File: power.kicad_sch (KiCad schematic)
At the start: 55 parts, among them Q1 AO3401A, Q2 AO3401A, Q21 FS8205A, Q6 2N7002, U10 BQ27546, U27 TPS63001, U29 BQ24081, U30 DW01+G, U6 TPS61040DBV

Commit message: Finish ESP32 fanout
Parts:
- added C41: 10uF, Capacitor_SMD:C_0402_1005Metric, symbol Device:C_Small
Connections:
- net GND: now also C41.1
- net at C41.2, D3.1 (K), Q1.2 (S)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: now also C41.2
- net VUSB renamed VBUS
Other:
- moved on the sheet: C41, C42, C43, L1, R9, U27

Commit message: Finish first layout revision
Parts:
- added R22: 100R, Resistor_SMD:R_0402_1005Metric, symbol Device:R_Small
- R22: footprint Resistor_SMD:R_0603_1608Metric -> Resistor_SMD:R_0402_1005Metric; LCSC C23179 -> C25117
- U10: footprint Package_DSBGA:DSBGA-15_1.95x2.6mm_P0.5mm -> Package_DSBGA:DSBGA-15_BQ27546_1.95x2.6mm_P0.5mm
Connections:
- net GND: now also U29.8 (~{TE})
- net VBUS: no longer U29.8 (~{TE})
- net at Q21.4, U30.1 (DO): now also R22.1
- net at C48.1, R22.2, U10.E1 (REGIN): no longer U10.D2 (CE)
- net at C48.1, C48.2, R22.2: now also U10.B1 (SRN); no longer U10.A2 (SRN)
- new net DSG: R22.2, U10.D2 (CE)
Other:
- moved on the sheet: C38, C47, R20

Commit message: Make EDRC happy (mostly)
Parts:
- C38: symbol Device:CP -> Device:C_Polarized
- FB1: symbol Device:Ferrite_Bead_Small -> Device:FerriteBead_Small
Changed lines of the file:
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@@
 (kicad_sch (version 20230121) (generator eeschema)
   (paper "A4")
+  (junction (at 148.59 143.51) (diameter 0) (color 0 0 0 0)
+  )
   (junction (at 101.6 163.83) (diameter 0) (color 0 0 0 0)
   )
@@
   (junction (at 172.72 163.83) (diameter 0) (color 0 0 0 0)
   )
-  (junction (at 115.57 46.99) (diameter 0) (color 0 0 0 0)
-  )
   (junction (at 38.1 46.99) (diameter 0) (color 0 0 0 0)
   )
@@
     (stroke (width 0) (type default))
   )
+  (wire (pts (xy 247.65 92.71) (xy 247.65 93.98))
+    (stroke (width 0) (type default))
+  )
   (wire (pts (xy 167.64 46.99) (xy 195.58 46.99))
     (stroke (width 0) (type default))
@@
     (stroke (width 0) (type default))
   )
-  (wire (pts (xy 137.16 143.51) (xy 151.13 143.51))
+  (wire (pts (xy 137.16 143.51) (xy 148.59 143.51))
+    (stroke (width 0) (type default))
+  )
+  (wire (pts (xy 148.59 142.24) (xy 148.59 143.51))
     (stroke (width 0) (type default))
   )
@@
     (stroke (width 0) (type default))
   )
-  (wire (pts (xy 151.13 154.94) (xy 151.13 163.83))
+  (wire (pts (xy 148.59 143.51) (xy 151.13 143.51))
     (stroke (width 0) (type default))
   )
-  (wire (pts (xy 115.57 38.1) (xy 115.57 46.99))
+  (wire (pts (xy 151.13 154.94) (xy 151.13 163.83))
     (stroke (width 0) (type default))
   )
@@
     (stroke (width 0) (type default))
   )
-  (wire (pts (xy 115.57 46.99) (xy 127 46.99))
+  (wire (pts (xy 142.24 86.36) (xy 142.24 87.63))
     (stroke (width 0) (type default))
   )
@@
     (stroke (width 0) (type default))
   )
+  (wire (pts (xy 207.01 81.28) (xy 207.01 82.55))
+    (stroke (width 0) (type default))
+  )
   (wire (pts (xy 240.03 46.99) (xy 250.19 46.99))
     (stroke (width 0) (type default))
@@
     (stroke (width 0) (type default))
   )
-  (wire (pts (xy 250.19 45.72) (xy 250.19 46.99))
-    (stroke (width 0) (type default))
-  )
   (wire (pts (xy 88.9 172.72) (xy 88.9 171.45))
     (stroke (width 0) (type default))
@@
     (stroke (width 0) (type default))
   )
-  (wire (pts (xy 106.68 46.99) (xy 115.57 46.99))
+  (wire (pts (xy 142.24 87.63) (xy 137.16 87.63))
+    (stroke (width 0) (type default))
+  )
+  (wire (pts (xy 106.68 46.99) (xy 127 46.99))
     (stroke (width 0) (type default))
   )
@@
     )
   )
-  (symbol (lib_id "Device:CP") (at 27.94 52.07 0) (unit 1)
+  (symbol (lib_id "Device:C_Polarized") (at 27.94 52.07 0) (unit 1)
     (in_bom yes) (on_board yes) (dnp no)
     (property "Reference" "C38" (at 30.9372 50.9016 0)
@@
     )
   )
-  (symbol (lib_name "+BATT_1") (lib_id "power:+BATT") (at 106.68 38.1 0) (unit 1)
+  (symbol (lib_id "power:+BATT") (at 106.68 38.1 0) (unit 1)
     (in_bom yes) (on_board yes) (dnp no) (fields_autoplaced)
     (property "Reference" "#PWR051" (at 106.68 41.91 0)
@@
     )
   )
+  (symbol (lib_id "power:PWR_FLAG") (at 207.01 81.28 0) (unit 1)
+    (in_bom yes) (on_board yes) (dnp no) (fields_autoplaced)
+    (property "Reference" "#FLG04" (at 207.01 79.375 0)
+      (effects (font (size 1.27 1.27)) hide)
+    )
+    (property "Value" "PWR_FLAG" (at 207.01 77.7781 0)
+      (effects (font (size 1.27 1.27)))
+    )
+    (property "Footprint" "" (at 207.01 81.28 0)
+      (effects (font (size 1.27 1.27)) hide)
+    )
+    (property "Datasheet" "~" (at 207.01 81.28 0)
+      (effects (font (size 1.27 1.27)) hide)
+    )
+    (pin "1")
+    (instances
+      (project "oled-nametag"
+        (path "/c0b8a503-1da4-4e1a-941c-dddf39a5c519/b1f1b085-615b-4d75-b80e-4b089a5e74f7"
+          (reference "#FLG04") (unit 1)
+        )
+      )
+    )
+  )
   (symbol (lib_id "Device:C_Small") (at 118.11 109.22 0) (mirror y) (unit 1)
     (in_bom yes) (on_board yes) (dnp no)
@@
     )
   )
+  (symbol (lib_id "power:PWR_FLAG") (at 148.59 142.24 0) (unit 1)
+    (in_bom yes) (on_board yes) (dnp no) (fields_autoplaced)
+    (property "Reference" "#FLG08" (at 148.59 140.335 0)
+      (effects (font (size 1.27 1.27)) hide)
+    )
+    (property "Value" "PWR_FLAG" (at 148.59 138.7381 0)
+      (effects (font (size 1.27 1.27)))
+    )
+    (property "Footprint" "" (at 148.59 142.24 0)
+      (effects (font (size 1.27 1.27)) hide)
+    )
+    (property "Datasheet" "~" (at 148.59 142.24 0)
+      (effects (font (size 1.27 1.27)) hide)
+    )
+    (pin "1")
+    (instances
+      (project "oled-nametag"
+        (path "/c0b8a503-1da4-4e1a-941c-dddf39a5c519/b1f1b085-615b-4d75-b80e-4b089a5e74f7"
+          (reference "#FLG08") (unit 1)
+        )
+      )
+    )
+  )
   (symbol (lib_id "Device:C_Small") (at 207.01 86.36 0) (mirror x) (unit 1)
     (in_bom yes) (on_board yes) (dnp no) (fields_autoplaced)
@@
     )
   )
+  (symbol (lib_id "power:PWR_FLAG") (at 142.24 86.36 0) (unit 1)
+    (in_bom yes) (on_board yes) (dnp no) (fields_autoplaced)
+    (property "Reference" "#FLG03" (at 142.24 84.455 0)
+      (effects (font (size 1.27 1.27)) hide)
+    )
+    (property "Value" "PWR_FLAG" (at 142.24 82.8581 0)
+      (effects (font (size 1.27 1.27)))
+    )
+    (property "Footprint" "" (at 142.24 86.36 0)
+      (effects (font (size 1.27 1.27)) hide)
+    )
+    (property "Datasheet" "~" (at 142.24 86.36 0)
+      (effects (font (size 1.27 1.27)) hide)
+    )
+    (pin "1")
+    (instances
+      (project "oled-nametag"
+        (path "/c0b8a503-1da4-4e1a-941c-dddf39a5c519/b1f1b085-615b-4d75-b80e-4b089a5e74f7"
+          (reference "#FLG03") (unit 1)
+        )
+      )
+    )
+  )
   (symbol (lib_id "power:GND") (at 213.36 68.58 0) (unit 1)
     (in_bom yes) (on_board yes) (dnp no)
@@
     )
   )
-  (symbol (lib_id "power:PWR_FLAG") (at 250.19 45.72 0) (unit 1)
-    (in_bom yes) (on_board yes) (dnp no) (fields_autoplaced)
-    (property "Reference" "#FLG04" (at 250.19 43.815 0)
+  (symbol (lib_id "power:GND") (at 38.1 64.77 0) (unit 1)
+    (in_bom yes) (on_board yes) (dnp no)
+    (property "Reference" "#PWR0209" (at 38.1 71.12 0)
       (effects (font (size 1.27 1.27)) hide)
     )
-    (property "Value" "PWR_FLAG" (at 250.19 42.2181 0)
+    (property "Value" "GND" (at 38.227 69.1642 0)
       (effects (font (size 1.27 1.27)))
     )
-    (property "Footprint" "" (at 250.19 45.72 0)
+    (property "Footprint" "" (at 38.1 64.77 0)
       (effects (font (size 1.27 1.27)) hide)
     )
-    (property "Datasheet" "~" (at 250.19 45.72 0)
+    (property "Datasheet" "" (at 38.1 64.77 0)
       (effects (font (size 1.27 1.27)) hide)
     )
     (pin "1")
     (instances
+      (project "rgb-led-nametag-48x16"
+        (path "/751d823e-1d7b-4501-9658-d06d459b0e16"
+          (reference "#PWR0209") (unit 1)
+        )
+      )
       (project "oled-nametag"
         (path "/c0b8a503-1da4-4e1a-941c-dddf39a5c519/b1f1b085-615b-4d75-b80e-4b089a5e74f7"
-          (reference "#FLG04") (unit 1)
+          (reference "#PWR046") (unit 1)
         )
       )
     )
   )
-  (symbol (lib_id "power:GND") (at 38.1 64.77 0) (unit 1)
-    (in_bom yes) (on_board yes) (dnp no)
-    (property "Reference" "#PWR0209" (at 38.1 71.12 0)
+  (symbol (lib_id "power:PWR_FLAG") (at 247.65 92.71 0) (unit 1)
+    (in_bom yes) (on_board yes) (dnp no) (fields_autoplaced)
+    (property "Reference" "#FLG09" (at 247.65 90.805 0)
       (effects (font (size 1.27 1.27)) hide)
     )
-    (property "Value" "GND" (at 38.227 69.1642 0)
+    (property "Value" "PWR_FLAG" (at 247.65 89.2081 0)
       (effects (font (size 1.27 1.27)))
     )
-    (property "Footprint" "" (at 38.1 64.77 0)
+    (property "Footprint" "" (at 247.65 92.71 0)
       (effects (font (size 1.27 1.27)) hide)
     )
-    (property "Datasheet" "" (at 38.1 64.77 0)
+    (property "Datasheet" "~" (at 247.65 92.71 0)
       (effects (font (size 1.27 1.27)) hide)
     )
     (pin "1")
     (instances
-      (project "rgb-led-nametag-48x16"
-        (path "/751d823e-1d7b-4501-9658-d06d459b0e16"
-          (reference "#PWR0209") (unit 1)
-        )
-      )
       (project "oled-nametag"
         (path "/c0b8a503-1da4-4e1a-941c-dddf39a5c519/b1f1b085-615b-4d75-b80e-4b089a5e74f7"
-          (reference "#PWR046") (unit 1)
+          (reference "#FLG09") (unit 1)
         )
       )
@@
     )
   )
-  (symbol (lib_id "power:PWR_FLAG") (at 115.57 38.1 0) (unit 1)
-    (in_bom yes) (on_board yes) (dnp no) (fields_autoplaced)
-    (property "Reference" "#FLG03" (at 115.57 36.195 0)
-      (effects (font (size 1.27 1.27)) hide)
-    )
-    (property "Value" "PWR_FLAG" (at 115.57 34.5981 0)
-      (effects (font (size 1.27 1.27)))
-    )
-    (property "Footprint" "" (at 115.57 38.1 0)
-      (effects (font (size 1.27 1.27)) hide)
-    )
-    (property "Datasheet" "~" (at 115.57 38.1 0)
-      (effects (font (size 1.27 1.27)) hide)
-    )
-    (pin "1")
-    (instances
-      (project "oled-nametag"
-        (path "/c0b8a503-1da4-4e1a-941c-dddf39a5c519/b1f1b085-615b-4d75-b80e-4b089a5e74f7"
-          (reference "#FLG03") (unit 1)
-        )
-      )
-    )
-  )
   (symbol (lib_id "power:GND") (at 222.25 105.41 0) (unit 1)
     (in_bom yes) (on_board yes) (dnp no) (fields_autoplaced)
@@
     )
   )
-  (symbol (lib_id "Device:Ferrite_Bead_Small") (at 36.83 30.48 90) (unit 1)
+  (symbol (lib_id "Device:FerriteBead_Small") (at 36.83 30.48 90) (unit 1)
     (in_bom yes) (on_board yes) (dnp no)
     (property "Reference" "FB1" (at 35.6616 27.94 0)

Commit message: Add fuel gauge thermistor
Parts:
- added R21: 10k, Resistor_SMD:R_0402_1005Metric, symbol Device:R_Small
- U10: footprint Package_DSBGA:DSBGA-15_BQ27546_1.95x2.6mm_P0.5mm -> Package_DSBGA:DSBGA-15_BQ27546_I2C_1.95x2.6mm_P0.5mm
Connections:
- net GND: now also R21.2
- net at U10.B2 (TS): now also R21.1
- no-connect marks 4 -> 3
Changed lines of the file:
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@@
   )
   (no_connect (at 146.05 100.33))
-  (no_connect (at 128.27 115.57))
   (no_connect (at 146.05 95.25))
   (no_connect (at 161.29 168.91))
@@
   )
   (wire (pts (xy 237.49 33.02) (xy 237.49 41.91))
+    (stroke (width 0) (type default))
+  )
+  (wire (pts (xy 128.27 115.57) (xy 128.27 118.11))
     (stroke (width 0) (type default))
   )
@@
     )
   )
+  (symbol (lib_id "power:GND") (at 128.27 123.19 0) (mirror y) (unit 1)
+    (in_bom yes) (on_board yes) (dnp no)
+    (property "Reference" "#PWR0210" (at 128.27 129.54 0)
+      (effects (font (size 1.27 1.27)) hide)
+    )
+    (property "Value" "GND" (at 128.143 127.5842 0)
+      (effects (font (size 1.27 1.27)))
+    )
+    (property "Footprint" "" (at 128.27 123.19 0)
+      (effects (font (size 1.27 1.27)) hide)
+    )
+    (property "Datasheet" "" (at 128.27 123.19 0)
+      (effects (font (size 1.27 1.27)) hide)
+    )
+    (pin "1")
+    (instances
+      (project "rgb-led-nametag-48x16"
+        (path "/751d823e-1d7b-4501-9658-d06d459b0e16"
+          (reference "#PWR0210") (unit 1)
+        )
+      )
+      (project "oled-nametag"
+        (path "/c0b8a503-1da4-4e1a-941c-dddf39a5c519/b1f1b085-615b-4d75-b80e-4b089a5e74f7"
+          (reference "#PWR035") (unit 1)
+        )
+      )
+    )
+  )
   (symbol (lib_id "power:+BATT") (at 106.68 38.1 0) (unit 1)
     (in_bom yes) (on_board yes) (dnp no) (fields_autoplaced)
@@
       (effects (font (size 1.27 1.27)) (justify left))
     )
-    (property "Footprint" "Package_DSBGA:DSBGA-15_BQ27546_1.95x2.6mm_P0.5mm" (at 137.16 104.14 0)
+    (property "Footprint" "Package_DSBGA:DSBGA-15_BQ27546_I2C_1.95x2.6mm_P0.5mm" (at 137.16 104.14 0)
       (effects (font (size 1.27 1.27)) hide)
     )
@@
         )
       )
+    )
+  )
+  (symbol (lib_id "Device:R_Small") (at 128.27 120.65 0) (unit 1)
+    (in_bom yes) (on_board yes) (dnp no)
+    (property "Reference" "R21" (at 126.7714 119.4816 0)
+      (effects (font (size 1.27 1.27)) (justify right))
+    )
+    (property "Value" "10k" (at 126.7714 121.793 0)
+      (effects (font (size 1.27 1.27)) (justify right))
+    )
+    (property "Footprint" "Resistor_SMD:R_0402_1005Metric" (at 128.27 120.65 0)
+      (effects (font (size 1.27 1.27)) hide)
+    )
+    (property "Datasheet" "~" (at 128.27 120.65 0)
+      (effects (font (size 1.27 1.27)) hide)
+    )
+    (property "LCSC" "C25744" (at 128.27 120.65 0)
+      (effects (font (size 1.27 1.27)) hide)
+    )
+    (pin "1")
+    (pin "2")
+    (instances
+      (project "rgb-led-nametag-48x16"
+        (path "/751d823e-1d7b-4501-9658-d06d459b0e16"
+          (reference "R21") (unit 1)
+        )
+      )
+      (project "oled-nametag"
+        (path "/c0b8a503-1da4-4e1a-941c-dddf39a5c519/b1f1b085-615b-4d75-b80e-4b089a5e74f7"
+          (reference "R33") (unit 1)
+        )
+      )

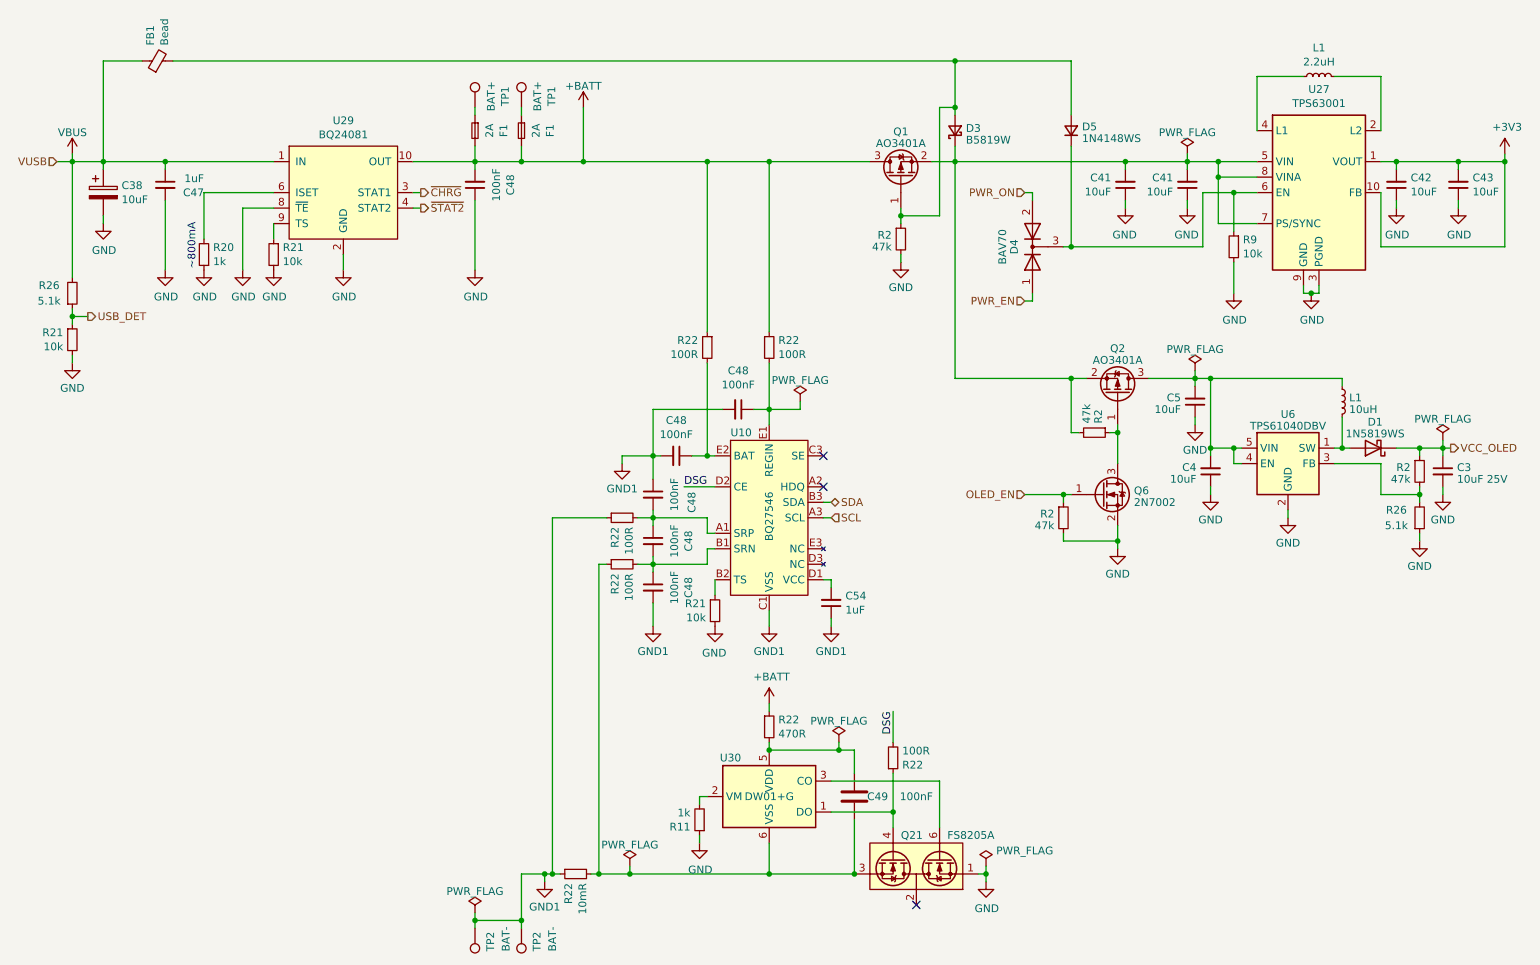
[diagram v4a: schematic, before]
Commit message: Add power rail testpoints
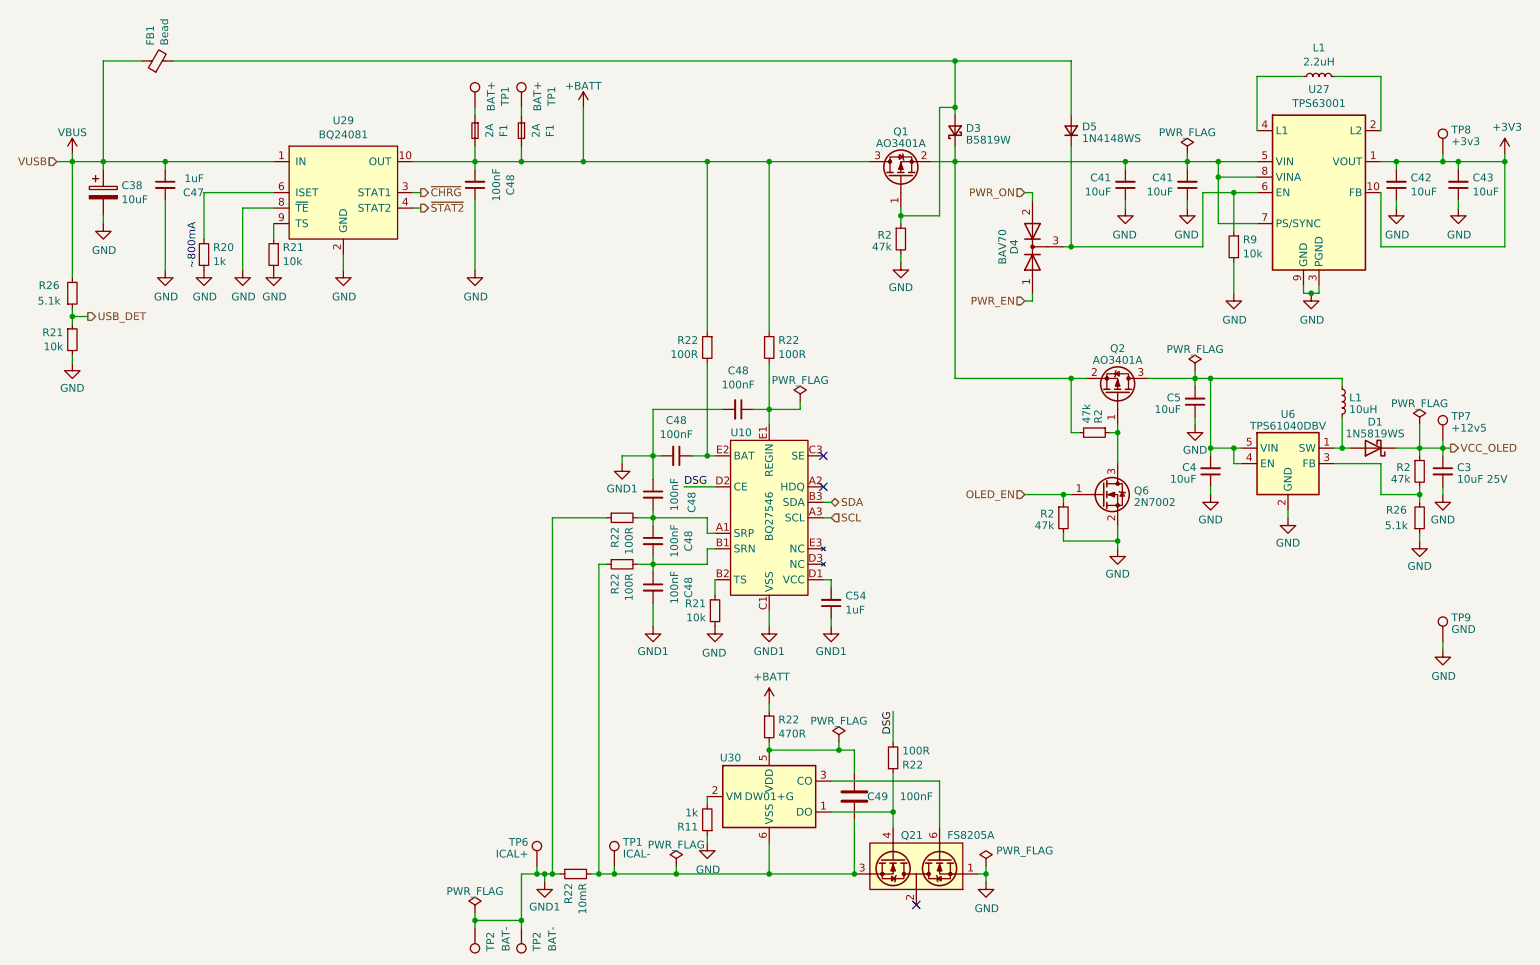
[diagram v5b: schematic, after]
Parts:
- added TP1: ICAL-, TestPoint:TestPoint_Pad_1.0x1.0mm, symbol Connector:TestPoint
- added TP6: ICAL+, TestPoint:TestPoint_Pad_1.0x1.0mm, symbol Connector:TestPoint
- added TP7: +12v5, TestPoint:TestPoint_Pad_1.0x1.0mm, symbol Connector:TestPoint
- added TP8: +3v3, TestPoint:TestPoint_Pad_1.0x1.0mm, symbol Connector:TestPoint
- added TP9: GND, TestPoint:TestPoint_Pad_1.0x1.0mm, symbol Connector:TestPoint
- TP1, TP2: now left out of the parts list
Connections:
- net +3V3: now also TP8.1
- net GND: now also TP9.1
- net GND1: now also TP6.1
- net VCC_OLED: now also TP7.1
- net at C49.1, Q21.3, R22.1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: now also TP1.1
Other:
- moved on the sheet: R11
